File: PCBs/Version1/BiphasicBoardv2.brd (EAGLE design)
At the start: 28.6 x 17.8 mm, 18 parts

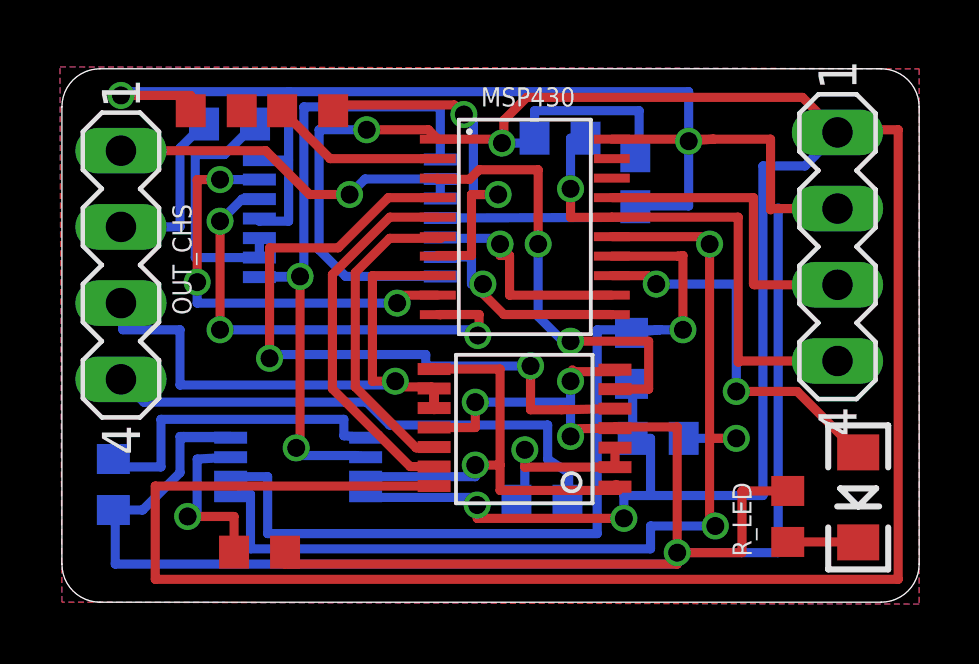
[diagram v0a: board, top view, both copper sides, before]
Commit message: Moved some wires around to make ground plane larger.
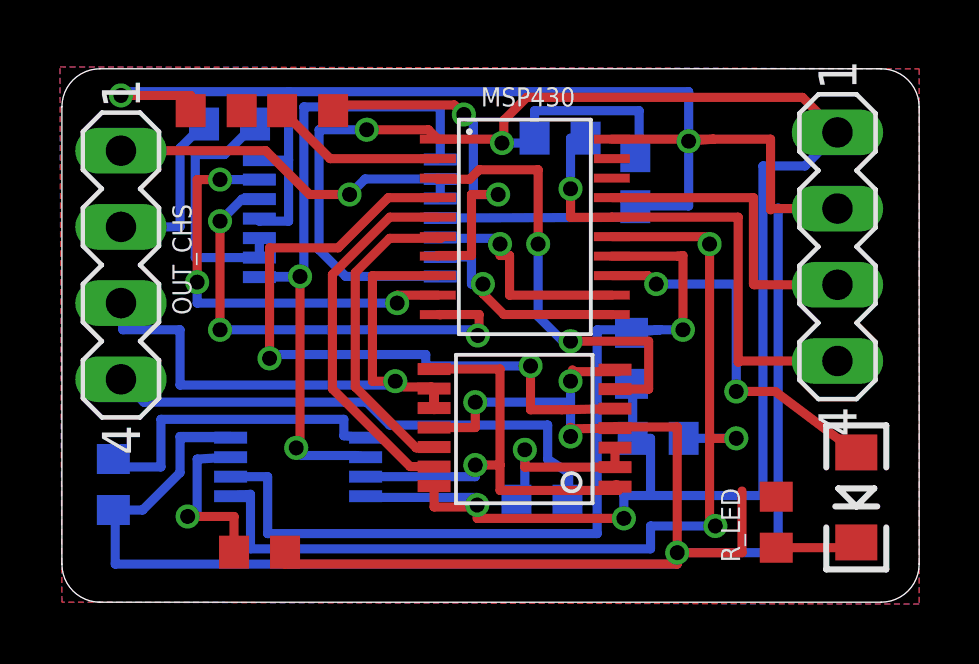
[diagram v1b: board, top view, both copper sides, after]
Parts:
- moved R_LED 0.43 mm to (23.8, 2.67)
- moved LED6 0.06 mm to (26.5, 3.49)
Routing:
- net VDD: track 122.5 -> 70.3 mm
- net GND: track 134.3 -> 132.8 mm
